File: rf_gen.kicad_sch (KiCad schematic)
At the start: 48 parts, among them J1 Conn_01x07_Male, J2 Conn_01x02_Female, J3 Conn_01x05_Male, J4 Jack-DC, Q1 GS61004B, Q2 G3R350MT12J, U1 NPC81074, U2 AP62150

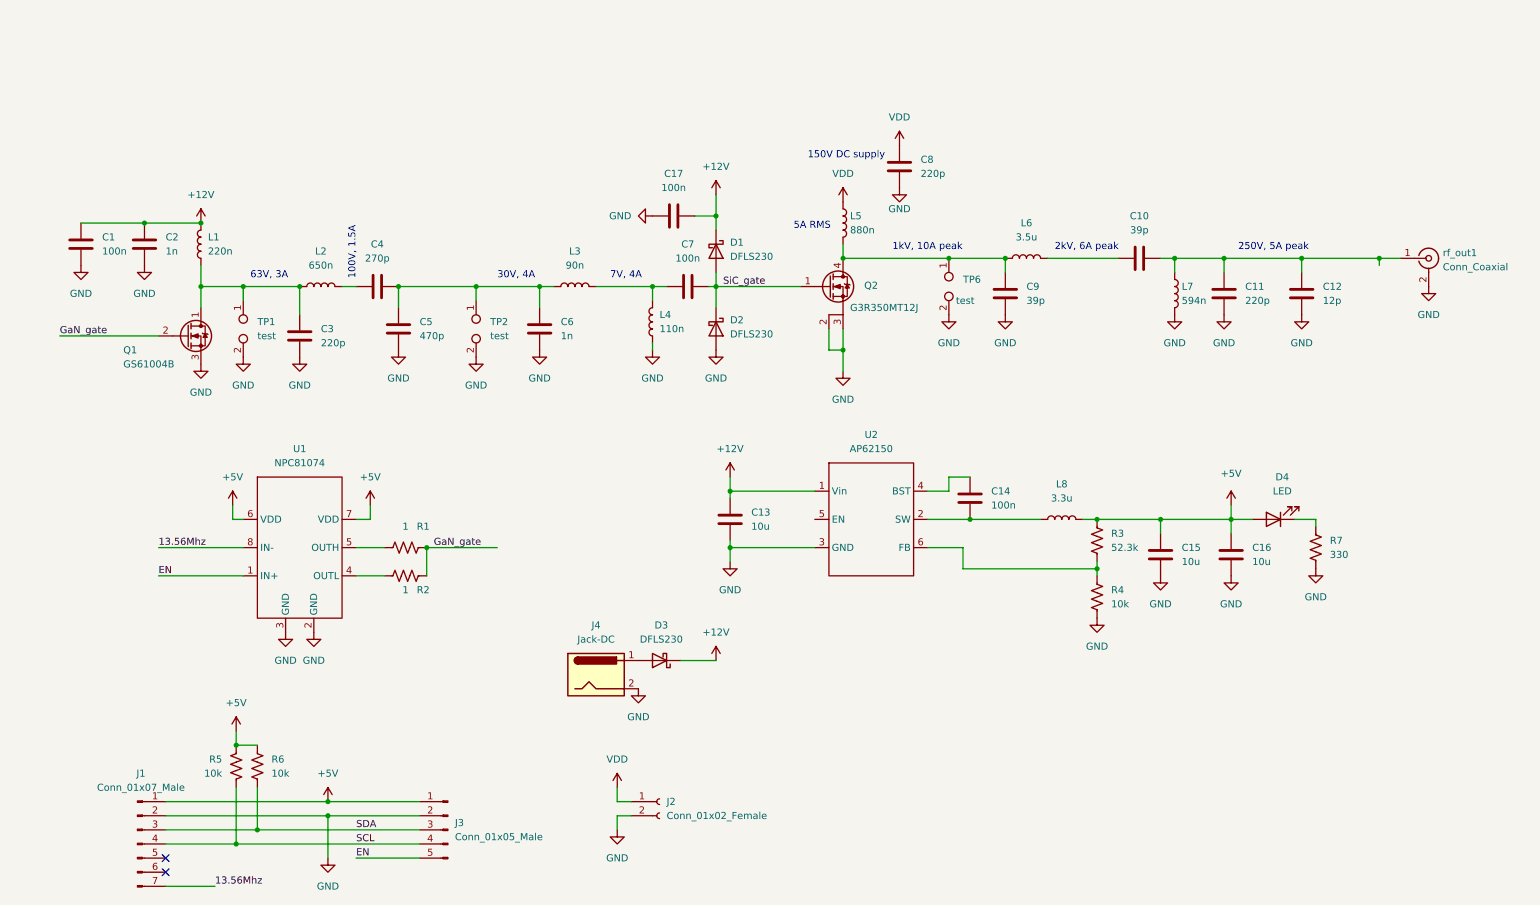
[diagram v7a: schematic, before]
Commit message: Added heatsink
Switched power inductors to surface-mount to avoid shorting
Added silkscreen text for connectors and LEDs
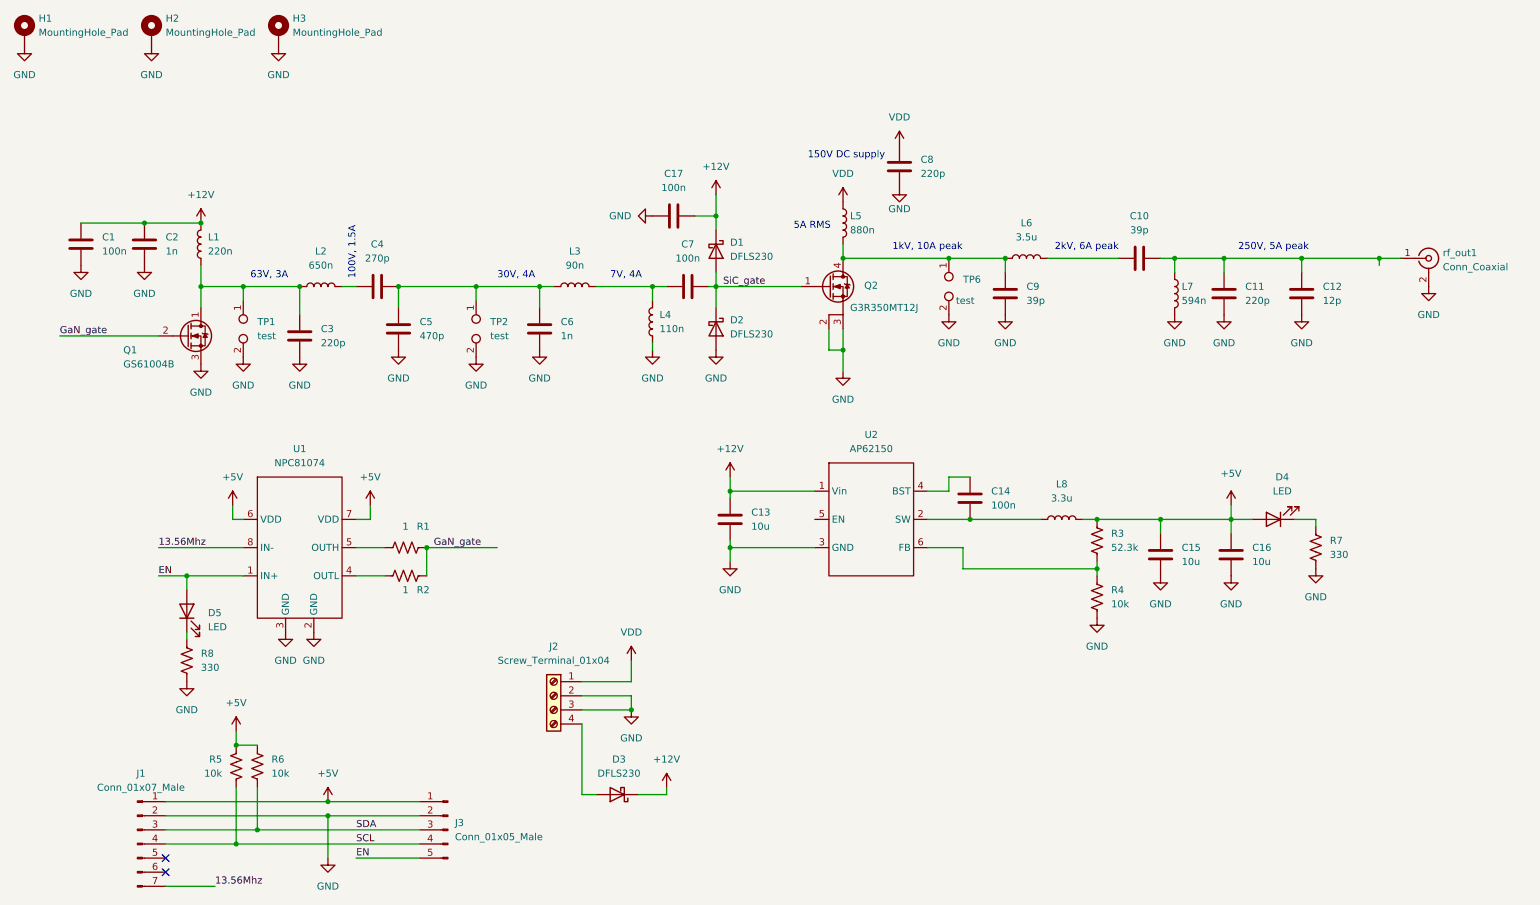
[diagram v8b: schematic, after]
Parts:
- removed J2: Conn_01x02_Female, Connector_Phoenix_MSTB:PhoenixContact_MSTBVA_2,5_2-G_1x02_P5.00mm_Vertical, symbol Connector:Conn_01x02_Female
- removed J4: Jack-DC, Connector_Phoenix_MSTB:PhoenixContact_MSTBVA_2,5_2-G_1x02_P5.00mm_Vertical, symbol Connector:Jack-DC
- added D5: LED, LED_SMD:LED_0805_2012Metric, symbol Device:LED
- added H1, H2, H3: MountingHole_Pad, MountingHole:MountingHole_3.2mm_M3_Pad_Via, symbol Mechanical:MountingHole_Pad
- added J2: Screw_Terminal_01x04, TerminalBlock_Phoenix:TerminalBlock_Phoenix_MKDS-1,5-4-5.08_1x04_P5.08mm_Horizontal, symbol Connector:Screw_Terminal_01x04
- added R8: 330, Resistor_SMD:R_0805_2012Metric, symbol Device:R_US
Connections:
- net EN: now also D5.2 (A)
- net GND: now also H1.1, H2.1, H3.1, J2.2 (Pin_2), J2.3 (Pin_3), R8.2
- net VDD: now also J2.1 (Pin_1)
- net at D3.2 (A): now also J2.4 (Pin_4)
- new net: D5.1 (K), R8.1
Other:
- moved on the sheet: D3
